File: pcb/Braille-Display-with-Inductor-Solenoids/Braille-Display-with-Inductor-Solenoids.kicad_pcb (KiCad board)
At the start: 2 copper layers, 100 x 100 mm, 190 parts, among them J1 Screw_Terminal_01x02, J2 Screw_Terminal_01x02, J3 Screw_Terminal_01x02, SW1 SW_Push, SW2 SW_Push, U1 RP2040-Zero, U10 AD116, U11 AD116, U12 AD116, U13 AD116, U14 AD116, U15 AD116, U16 AD116, U17 AD116, U18 AD116, U19 AD116, U2 AD116, U20 AD116, U21 AD116, U22 AD116, U23 AD116, U24 AD116, U25 AD116, U3 AD116, U4 AD116, U5 AD116, U6 AD116, U7 AD116, U8 AD116, U9 AD116

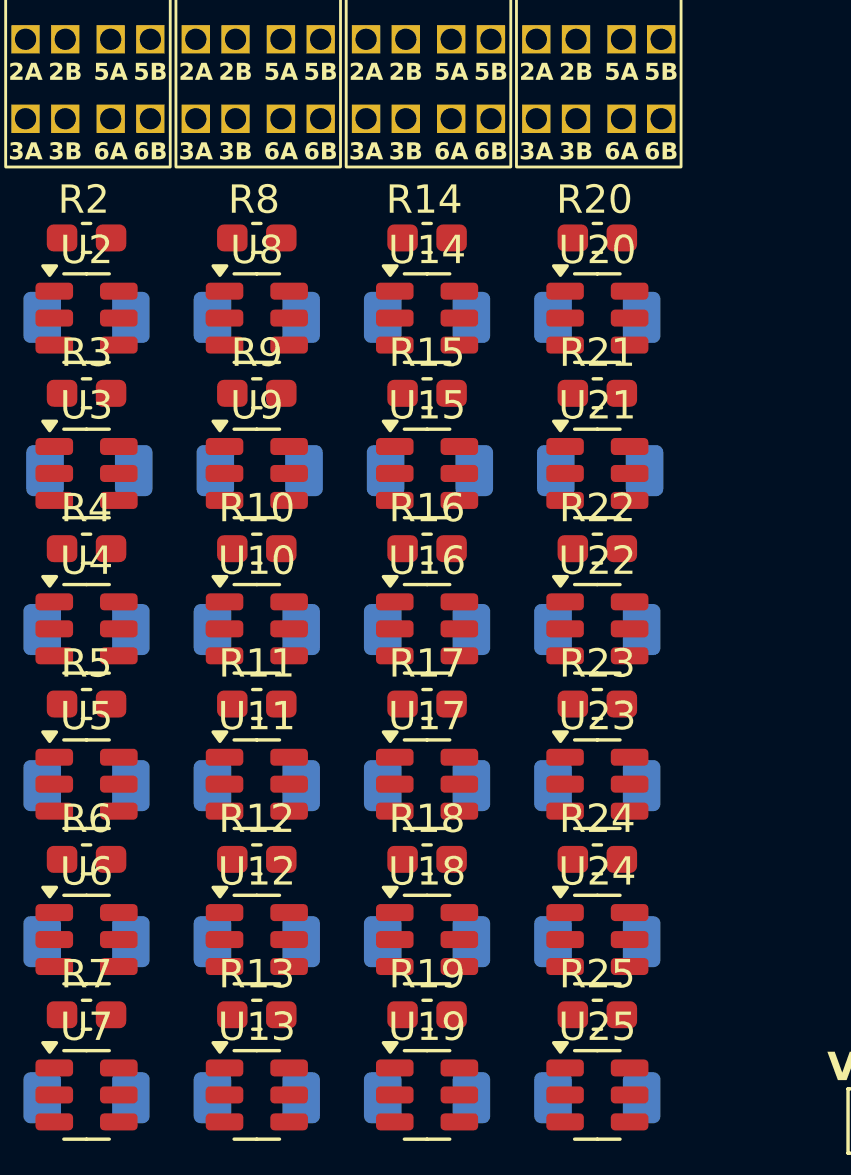
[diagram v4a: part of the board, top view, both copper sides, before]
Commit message: Change page layout and reconnect components
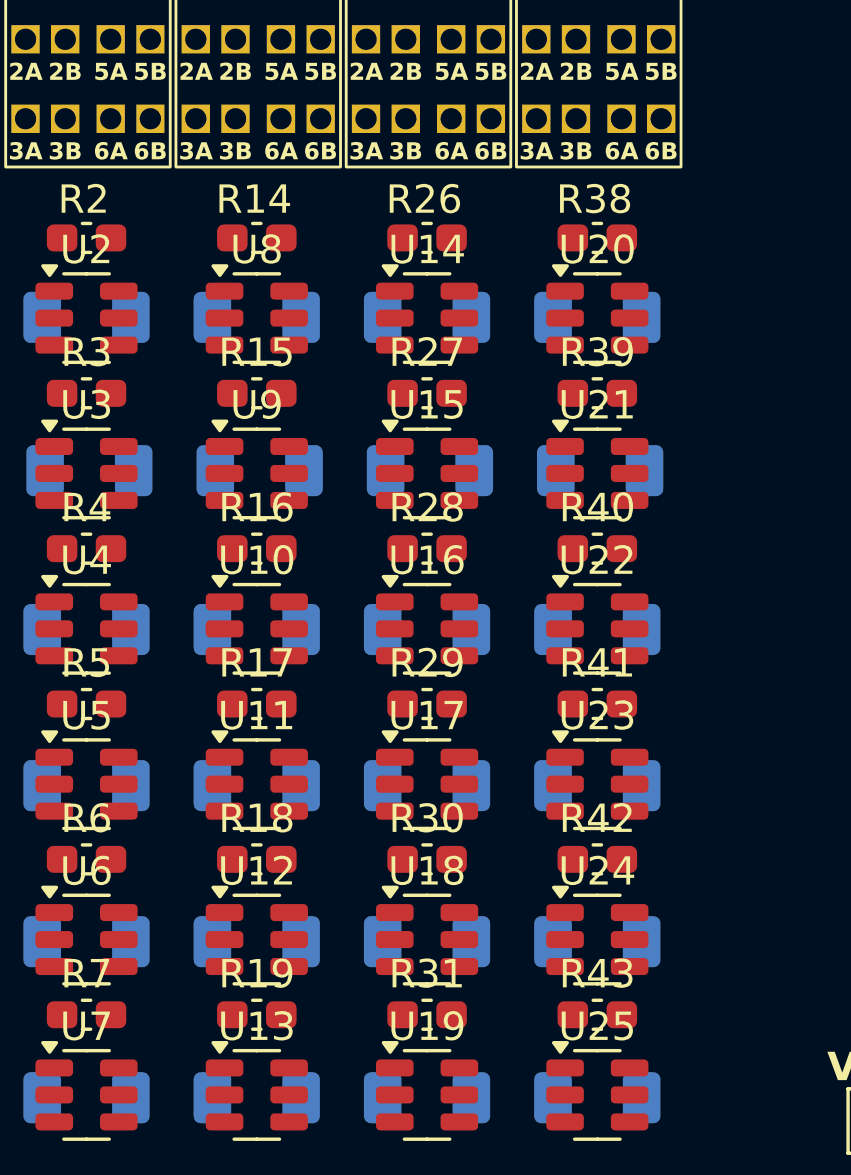
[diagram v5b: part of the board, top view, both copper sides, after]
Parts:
- R10, R11, R12, R13, R20, R21, R22, R23, R24, R25, R8, R9: value 20 -> 5k1; footprint Capacitor_SMD:C_0603_1608Metric_Pad1.08x0.95mm_HandSolder -> Resistor_SMD:R_0603_1608Metric; moved to B.Cu
- R26, R27, R28, R29, R30, R31, R38, R39, R40, R41, R42, R43: value 5k1 -> 20; footprint Resistor_SMD:R_0603_1608Metric -> Capacitor_SMD:C_0603_1608Metric_Pad1.08x0.95mm_HandSolder; moved to F.Cu
- moved R38 40.5 mm to (69.2, 71.0), turned to 180 degrees
- moved R20 36.5 mm to (57.2, 105.5)
- moved R26 36.5 mm to (63.2, 71.0)
- moved R8 35.0 mm to (51.2, 105.5)
- moved R21 34.9 mm to (57.1, 109.2), turned to 180 degrees
- moved R9 33.3 mm to (51.1, 109.2), turned to 180 degrees
- moved R22 33.2 mm to (57.1, 112.9), turned to 180 degrees
- moved R39 33.1 mm to (69.2, 76.5)
- moved C5 32.9 mm to (51.2, 101.3)
- moved R10 31.5 mm to (51.1, 112.9), turned to 180 degrees
- moved R27 29.6 mm to (63.2, 76.5), turned to 0 degrees
- moved R40 26.1 mm to (69.2, 82.0)
- moved R42 25.6 mm to (69.2, 92.9)
- moved C4 25.1 mm to (51.2, 95.8)
- moved R28 23.5 mm to (63.2, 82.0), turned to 0 degrees
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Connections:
- net /Braille_Cell/DOT1_A renamed /Braille_Cells_and_Controls/Braille_Cell/DOT1_A
- net /Braille_Cell/DOT1_B renamed /Braille_Cells_and_Controls/Braille_Cell/DOT1_B
- net /Braille_Cell/DOT1_B_CTRL renamed /Braille_Cells_and_Controls/CELL0_DOT1_B
- net /Braille_Cell/DOT2_A renamed /Braille_Cells_and_Controls/Braille_Cell/DOT2_A
- net /Braille_Cell/DOT2_B renamed /Braille_Cells_and_Controls/Braille_Cell/DOT2_B
- net /Braille_Cell/DOT3_A renamed /Braille_Cells_and_Controls/Braille_Cell/DOT3_A
- net /Braille_Cell/DOT3_B renamed /Braille_Cells_and_Controls/Braille_Cell/DOT3_B
- net /Braille_Cell/DOT4_A renamed /Braille_Cells_and_Controls/Braille_Cell/DOT4_A
- net /Braille_Cell/DOT4_B renamed /Braille_Cells_and_Controls/Braille_Cell/DOT4_B
- net /Braille_Cell/DOT5_A renamed /Braille_Cells_and_Controls/Braille_Cell/DOT5_A
- net /Braille_Cell/DOT5_B renamed /Braille_Cells_and_Controls/Braille_Cell/DOT5_B
- net /Braille_Cell/DOT6_A renamed /Braille_Cells_and_Controls/Braille_Cell/DOT6_A
- net /Braille_Cell/DOT6_B renamed /Braille_Cells_and_Controls/Braille_Cell/DOT6_B
- net /Braille_Cell1/DOT1_A renamed /Braille_Cells_and_Controls/Braille_Cell1/DOT1_A
- net /Braille_Cell1/DOT2_A renamed /Braille_Cells_and_Controls/Braille_Cell1/DOT2_A
- net /Braille_Cell1/DOT3_A renamed /Braille_Cells_and_Controls/Braille_Cell1/DOT3_A
- net /Braille_Cell1/DOT4_A renamed /Braille_Cells_and_Controls/Braille_Cell1/DOT4_A
- net /Braille_Cell1/DOT5_A renamed /Braille_Cells_and_Controls/Braille_Cell1/DOT5_A
- net /Braille_Cell1/DOT6_A renamed /Braille_Cells_and_Controls/Braille_Cell1/DOT6_A
- net /Braille_Cell2/DOT1_A renamed /Braille_Cells_and_Controls/Braille_Cell2/DOT1_A
- net /Braille_Cell2/DOT2_A renamed /Braille_Cells_and_Controls/Braille_Cell2/DOT2_A
- net /Braille_Cell2/DOT3_A renamed /Braille_Cells_and_Controls/Braille_Cell2/DOT3_A
- net /Braille_Cell2/DOT4_A renamed /Braille_Cells_and_Controls/Braille_Cell2/DOT4_A
- net /Braille_Cell2/DOT5_A renamed /Braille_Cells_and_Controls/Braille_Cell2/DOT5_A
- net /Braille_Cell2/DOT6_A renamed /Braille_Cells_and_Controls/Braille_Cell2/DOT6_A
- net /Braille_Cell3/DOT1_A renamed /Braille_Cells_and_Controls/Braille_Cell3/DOT1_A
- net /Braille_Cell3/DOT2_A renamed /Braille_Cells_and_Controls/Braille_Cell3/DOT2_A
- net /Braille_Cell3/DOT3_A renamed /Braille_Cells_and_Controls/Braille_Cell3/DOT3_A
- net /Braille_Cell3/DOT4_A renamed /Braille_Cells_and_Controls/Braille_Cell3/DOT4_A
- net /Braille_Cell3/DOT5_A renamed /Braille_Cells_and_Controls/Braille_Cell3/DOT5_A
- net /Braille_Cell3/DOT6_A renamed /Braille_Cells_and_Controls/Braille_Cell3/DOT6_A
- net /Braille_Cell3/DOT6_A_CTRL renamed /Braille_Cells_and_Controls/CELL3_DOT6_A
- net /Braille_Cell3/DOT6_B_CTRL renamed /Braille_Cells_and_Controls/CELL3_DOT6_B
- D10 pad 1: /Braille_Cell/DOT2_B_CTRL -> /Braille_Cells_and_Controls/CELL1_DOT3_B
- D11 pad 1: /Braille_Cell/DOT5_B_CTRL -> /Braille_Cells_and_Controls/CELL1_DOT4_B
- D12 pad 1: /Braille_Cell1/DOT2_B_CTRL -> /Braille_Cells_and_Controls/CELL1_DOT5_B
- D13 pad 1: /Braille_Cell1/DOT5_B_CTRL -> /Braille_Cells_and_Controls/CELL1_DOT6_B
- D14 pad 1: /Braille_Cell2/DOT2_B_CTRL -> /Braille_Cells_and_Controls/CELL2_DOT1_B
- D15 pad 1: /Braille_Cell2/DOT5_B_CTRL -> /Braille_Cells_and_Controls/CELL2_DOT2_B
- D16 pad 1: /Braille_Cell3/DOT2_B_CTRL -> /Braille_Cells_and_Controls/CELL2_DOT3_B
- D17 pad 1: /Braille_Cell3/DOT5_B_CTRL -> /Braille_Cells_and_Controls/CELL2_DOT4_B
- D18 pad 1: /Braille_Cell/DOT3_B_CTRL -> /Braille_Cells_and_Controls/CELL2_DOT5_B
- D19 pad 1: /Braille_Cell/DOT6_B_CTRL -> /Braille_Cells_and_Controls/CELL2_DOT6_B
- D20 pad 1: /Braille_Cell1/DOT3_B_CTRL -> /Braille_Cells_and_Controls/CELL3_DOT1_B
- D21 pad 1: /Braille_Cell1/DOT6_B_CTRL -> /Braille_Cells_and_Controls/CELL3_DOT2_B
- D22 pad 1: /Braille_Cell2/DOT3_B_CTRL -> /Braille_Cells_and_Controls/CELL3_DOT3_B
- D23 pad 1: /Braille_Cell2/DOT6_B_CTRL -> /Braille_Cells_and_Controls/CELL3_DOT4_B
- D24 pad 1: /Braille_Cell3/DOT3_B_CTRL -> /Braille_Cells_and_Controls/CELL3_DOT5_B
- D3 pad 1: /Braille_Cell1/DOT1_B_CTRL -> /Braille_Cells_and_Controls/CELL0_DOT2_B
- D4 pad 1: /Braille_Cell2/DOT1_B_CTRL -> /Braille_Cells_and_Controls/CELL0_DOT3_B
- D5 pad 1: /Braille_Cell3/DOT1_B_CTRL -> /Braille_Cells_and_Controls/CELL0_DOT4_B
- D6 pad 1: /Braille_Cell/DOT4_B_CTRL -> /Braille_Cells_and_Controls/CELL0_DOT5_B
- D7 pad 1: /Braille_Cell1/DOT4_B_CTRL -> /Braille_Cells_and_Controls/CELL0_DOT6_B
- D8 pad 1: /Braille_Cell2/DOT4_B_CTRL -> /Braille_Cells_and_Controls/CELL1_DOT1_B
- D9 pad 1: /Braille_Cell3/DOT4_B_CTRL -> /Braille_Cells_and_Controls/CELL1_DOT2_B
- R10 pad 1: /Braille_Cell1/DOT3_B -> /Braille_Cells_and_Controls/CELL0_DOT3_A
- R10 pad 2: Net-(B2-3B) -> Net-(D4-AK)
- R11 pad 1: Net-(B2-4B) -> /Braille_Cells_and_Controls/CELL0_DOT4_A
- R11 pad 2: /Braille_Cell1/DOT4_B -> Net-(D5-AK)
- R12 pad 1: Net-(B2-5B) -> /Braille_Cells_and_Controls/CELL0_DOT5_A
- R12 pad 2: /Braille_Cell1/DOT5_B -> Net-(D6-AK)
- R13 pad 1: Net-(B2-6B) -> /Braille_Cells_and_Controls/CELL0_DOT6_A
- R13 pad 2: /Braille_Cell1/DOT6_B -> Net-(D7-AK)
- R14 pad 1: /Braille_Cell2/DOT1_B -> /Braille_Cells_and_Controls/Braille_Cell1/DOT1_B
- R14 pad 2: Net-(B3-1B) -> Net-(B2-1B)
- R15 pad 1: /Braille_Cell2/DOT2_B -> /Braille_Cells_and_Controls/Braille_Cell1/DOT2_B
- R15 pad 2: Net-(B3-2B) -> Net-(B2-2B)
- R16 pad 1: /Braille_Cell2/DOT3_B -> /Braille_Cells_and_Controls/Braille_Cell1/DOT3_B
- R16 pad 2: Net-(B3-3B) -> Net-(B2-3B)
- R17 pad 1: Net-(B3-4B) -> Net-(B2-4B)
- R17 pad 2: /Braille_Cell2/DOT4_B -> /Braille_Cells_and_Controls/Braille_Cell1/DOT4_B
- R18 pad 1: Net-(B3-5B) -> Net-(B2-5B)
- R18 pad 2: /Braille_Cell2/DOT5_B -> /Braille_Cells_and_Controls/Braille_Cell1/DOT5_B
- R19 pad 1: Net-(B3-6B) -> Net-(B2-6B)
- R19 pad 2: /Braille_Cell2/DOT6_B -> /Braille_Cells_and_Controls/Braille_Cell1/DOT6_B
- R20 pad 1: /Braille_Cell3/DOT1_B -> /Braille_Cells_and_Controls/CELL1_DOT1_A
- R20 pad 2: Net-(B4-1B) -> Net-(D8-AK)
- R21 pad 1: /Braille_Cell3/DOT2_B -> /Braille_Cells_and_Controls/CELL1_DOT2_A
- R21 pad 2: Net-(B4-2B) -> Net-(D9-AK)
- R22 pad 1: /Braille_Cell3/DOT3_B -> /Braille_Cells_and_Controls/CELL1_DOT3_A
- R22 pad 2: Net-(B4-3B) -> Net-(D10-AK)
- R23 pad 1: Net-(B4-4B) -> /Braille_Cells_and_Controls/CELL1_DOT4_A
- R23 pad 2: /Braille_Cell3/DOT4_B -> Net-(D11-AK)
- R24 pad 1: Net-(B4-5B) -> /Braille_Cells_and_Controls/CELL1_DOT5_A
- R24 pad 2: /Braille_Cell3/DOT5_B -> Net-(D12-AK)
- R25 pad 1: Net-(B4-6B) -> /Braille_Cells_and_Controls/CELL1_DOT6_A
- R25 pad 2: /Braille_Cell3/DOT6_B -> Net-(D13-AK)
- R26 pad 1: /Braille_Cell/DOT1_A_CTRL -> /Braille_Cells_and_Controls/Braille_Cell2/DOT1_B
- R26 pad 2: Net-(D2-AK) -> Net-(B3-1B)
- R27 pad 1: /Braille_Cell1/DOT1_A_CTRL -> /Braille_Cells_and_Controls/Braille_Cell2/DOT2_B
- R27 pad 2: Net-(D3-AK) -> Net-(B3-2B)
- R28 pad 1: /Braille_Cell2/DOT1_A_CTRL -> /Braille_Cells_and_Controls/Braille_Cell2/DOT3_B
- R28 pad 2: Net-(D4-AK) -> Net-(B3-3B)
- R29 pad 1: /Braille_Cell3/DOT1_A_CTRL -> Net-(B3-4B)
- R29 pad 2: Net-(D5-AK) -> /Braille_Cells_and_Controls/Braille_Cell2/DOT4_B
- R30 pad 1: /Braille_Cell/DOT2_A_CTRL -> Net-(B3-5B)
- R30 pad 2: Net-(D10-AK) -> /Braille_Cells_and_Controls/Braille_Cell2/DOT5_B
- R31 pad 1: /Braille_Cell1/DOT2_A_CTRL -> Net-(B3-6B)
- R31 pad 2: Net-(D12-AK) -> /Braille_Cells_and_Controls/Braille_Cell2/DOT6_B
- R32 pad 1: /Braille_Cell2/DOT2_A_CTRL -> /Braille_Cells_and_Controls/CELL2_DOT1_A
- R33 pad 1: /Braille_Cell3/DOT2_A_CTRL -> /Braille_Cells_and_Controls/CELL2_DOT2_A
- R33 pad 2: Net-(D16-AK) -> Net-(D15-AK)
- R34 pad 1: /Braille_Cell/DOT3_A_CTRL -> /Braille_Cells_and_Controls/CELL2_DOT3_A
- R34 pad 2: Net-(D18-AK) -> Net-(D16-AK)
- R35 pad 1: /Braille_Cell1/DOT3_A_CTRL -> /Braille_Cells_and_Controls/CELL2_DOT4_A
- R35 pad 2: Net-(D20-AK) -> Net-(D17-AK)
- R36 pad 1: /Braille_Cell2/DOT3_A_CTRL -> /Braille_Cells_and_Controls/CELL2_DOT5_A
- R36 pad 2: Net-(D22-AK) -> Net-(D18-AK)
- R37 pad 1: /Braille_Cell3/DOT3_A_CTRL -> /Braille_Cells_and_Controls/CELL2_DOT6_A
- R37 pad 2: Net-(D24-AK) -> Net-(D19-AK)
- R38 pad 1: /Braille_Cell/DOT4_A_CTRL -> /Braille_Cells_and_Controls/Braille_Cell3/DOT1_B
- R38 pad 2: Net-(D6-AK) -> Net-(B4-1B)
- R39 pad 1: /Braille_Cell1/DOT4_A_CTRL -> /Braille_Cells_and_Controls/Braille_Cell3/DOT2_B
- R39 pad 2: Net-(D7-AK) -> Net-(B4-2B)
- R40 pad 1: /Braille_Cell2/DOT4_A_CTRL -> /Braille_Cells_and_Controls/Braille_Cell3/DOT3_B
- R40 pad 2: Net-(D8-AK) -> Net-(B4-3B)
- R41 pad 1: /Braille_Cell3/DOT4_A_CTRL -> Net-(B4-4B)
- R41 pad 2: Net-(D9-AK) -> /Braille_Cells_and_Controls/Braille_Cell3/DOT4_B
- R42 pad 1: /Braille_Cell/DOT5_A_CTRL -> Net-(B4-5B)
- R42 pad 2: Net-(D11-AK) -> /Braille_Cells_and_Controls/Braille_Cell3/DOT5_B
- R43 pad 1: /Braille_Cell1/DOT5_A_CTRL -> Net-(B4-6B)
- R43 pad 2: Net-(D13-AK) -> /Braille_Cells_and_Controls/Braille_Cell3/DOT6_B
- R44 pad 1: /Braille_Cell2/DOT5_A_CTRL -> /Braille_Cells_and_Controls/CELL3_DOT1_A
- R44 pad 2: Net-(D15-AK) -> Net-(D20-AK)
- R45 pad 1: /Braille_Cell3/DOT5_A_CTRL -> /Braille_Cells_and_Controls/CELL3_DOT2_A
- R45 pad 2: Net-(D17-AK) -> Net-(D21-AK)
- R46 pad 1: /Braille_Cell/DOT6_A_CTRL -> /Braille_Cells_and_Controls/CELL3_DOT3_A
- R46 pad 2: Net-(D19-AK) -> Net-(D22-AK)
- R47 pad 1: /Braille_Cell1/DOT6_A_CTRL -> /Braille_Cells_and_Controls/CELL3_DOT4_A
- R47 pad 2: Net-(D21-AK) -> Net-(D23-AK)
- R48 pad 1: /Braille_Cell2/DOT6_A_CTRL -> /Braille_Cells_and_Controls/CELL3_DOT5_A
- R48 pad 2: Net-(D23-AK) -> Net-(D24-AK)
- R8 pad 1: /Braille_Cell1/DOT1_B -> /Braille_Cells_and_Controls/CELL0_DOT1_A
- R8 pad 2: Net-(B2-1B) -> Net-(D2-AK)
- R9 pad 1: /Braille_Cell1/DOT2_B -> /Braille_Cells_and_Controls/CELL0_DOT2_A
- R9 pad 2: Net-(B2-2B) -> Net-(D3-AK)
- U1 pad 14: /SHIFT_RCLK -> /~{SHIFT_SRCLR}
- U1 pad 15: /SHIFT_G -> /SHIFT_RCLK
- U1 pad 16: unconnected-(U1-GP6-Pad16)_1 -> /~{SHIFT_OE}
- U10 pad 1: /Braille_Cell1/DOT3_B -> /Braille_Cells_and_Controls/Braille_Cell1/DOT3_B
- U10 pad 3: /Braille_Cell1/DOT3_B_CTRL -> /Braille_Cells_and_Controls/CELL1_DOT3_B
- U10 pad 4: /Braille_Cell1/DOT3_A_CTRL -> /Braille_Cells_and_Controls/CELL1_DOT3_A
- U11 pad 1: /Braille_Cell1/DOT4_B -> /Braille_Cells_and_Controls/Braille_Cell1/DOT4_B
- U11 pad 3: /Braille_Cell1/DOT4_B_CTRL -> /Braille_Cells_and_Controls/CELL1_DOT4_B
- U11 pad 4: /Braille_Cell1/DOT4_A_CTRL -> /Braille_Cells_and_Controls/CELL1_DOT4_A
- U12 pad 1: /Braille_Cell1/DOT5_B -> /Braille_Cells_and_Controls/Braille_Cell1/DOT5_B
- U12 pad 3: /Braille_Cell1/DOT5_B_CTRL -> /Braille_Cells_and_Controls/CELL1_DOT5_B
- U12 pad 4: /Braille_Cell1/DOT5_A_CTRL -> /Braille_Cells_and_Controls/CELL1_DOT5_A
- U13 pad 1: /Braille_Cell1/DOT6_B -> /Braille_Cells_and_Controls/Braille_Cell1/DOT6_B
- U13 pad 3: /Braille_Cell1/DOT6_B_CTRL -> /Braille_Cells_and_Controls/CELL1_DOT6_B
- U13 pad 4: /Braille_Cell1/DOT6_A_CTRL -> /Braille_Cells_and_Controls/CELL1_DOT6_A
- U14 pad 1: /Braille_Cell2/DOT1_B -> /Braille_Cells_and_Controls/Braille_Cell2/DOT1_B
- U14 pad 3: /Braille_Cell2/DOT1_B_CTRL -> /Braille_Cells_and_Controls/CELL2_DOT1_B
- U14 pad 4: /Braille_Cell2/DOT1_A_CTRL -> /Braille_Cells_and_Controls/CELL2_DOT1_A
- U15 pad 1: /Braille_Cell2/DOT2_B -> /Braille_Cells_and_Controls/Braille_Cell2/DOT2_B
- U15 pad 3: /Braille_Cell2/DOT2_B_CTRL -> /Braille_Cells_and_Controls/CELL2_DOT2_B
- U15 pad 4: /Braille_Cell2/DOT2_A_CTRL -> /Braille_Cells_and_Controls/CELL2_DOT2_A
- U16 pad 1: /Braille_Cell2/DOT3_B -> /Braille_Cells_and_Controls/Braille_Cell2/DOT3_B
- U16 pad 3: /Braille_Cell2/DOT3_B_CTRL -> /Braille_Cells_and_Controls/CELL2_DOT3_B
- U16 pad 4: /Braille_Cell2/DOT3_A_CTRL -> /Braille_Cells_and_Controls/CELL2_DOT3_A
- U17 pad 1: /Braille_Cell2/DOT4_B -> /Braille_Cells_and_Controls/Braille_Cell2/DOT4_B
- U17 pad 3: /Braille_Cell2/DOT4_B_CTRL -> /Braille_Cells_and_Controls/CELL2_DOT4_B
- U17 pad 4: /Braille_Cell2/DOT4_A_CTRL -> /Braille_Cells_and_Controls/CELL2_DOT4_A
- U18 pad 1: /Braille_Cell2/DOT5_B -> /Braille_Cells_and_Controls/Braille_Cell2/DOT5_B
- U18 pad 3: /Braille_Cell2/DOT5_B_CTRL -> /Braille_Cells_and_Controls/CELL2_DOT5_B
- U18 pad 4: /Braille_Cell2/DOT5_A_CTRL -> /Braille_Cells_and_Controls/CELL2_DOT5_A
- U19 pad 1: /Braille_Cell2/DOT6_B -> /Braille_Cells_and_Controls/Braille_Cell2/DOT6_B
- U19 pad 3: /Braille_Cell2/DOT6_B_CTRL -> /Braille_Cells_and_Controls/CELL2_DOT6_B
- U19 pad 4: /Braille_Cell2/DOT6_A_CTRL -> /Braille_Cells_and_Controls/CELL2_DOT6_A
- U2 pad 4: /Braille_Cell/DOT1_A_CTRL -> /Braille_Cells_and_Controls/CELL0_DOT1_A
- U20 pad 1: /Braille_Cell3/DOT1_B -> /Braille_Cells_and_Controls/Braille_Cell3/DOT1_B
- U20 pad 3: /Braille_Cell3/DOT1_B_CTRL -> /Braille_Cells_and_Controls/CELL3_DOT1_B
- U20 pad 4: /Braille_Cell3/DOT1_A_CTRL -> /Braille_Cells_and_Controls/CELL3_DOT1_A
- U21 pad 1: /Braille_Cell3/DOT2_B -> /Braille_Cells_and_Controls/Braille_Cell3/DOT2_B
- U21 pad 3: /Braille_Cell3/DOT2_B_CTRL -> /Braille_Cells_and_Controls/CELL3_DOT2_B
- U21 pad 4: /Braille_Cell3/DOT2_A_CTRL -> /Braille_Cells_and_Controls/CELL3_DOT2_A
- U22 pad 1: /Braille_Cell3/DOT3_B -> /Braille_Cells_and_Controls/Braille_Cell3/DOT3_B
- U22 pad 3: /Braille_Cell3/DOT3_B_CTRL -> /Braille_Cells_and_Controls/CELL3_DOT3_B
- U22 pad 4: /Braille_Cell3/DOT3_A_CTRL -> /Braille_Cells_and_Controls/CELL3_DOT3_A
- U23 pad 1: /Braille_Cell3/DOT4_B -> /Braille_Cells_and_Controls/Braille_Cell3/DOT4_B
- U23 pad 3: /Braille_Cell3/DOT4_B_CTRL -> /Braille_Cells_and_Controls/CELL3_DOT4_B
- U23 pad 4: /Braille_Cell3/DOT4_A_CTRL -> /Braille_Cells_and_Controls/CELL3_DOT4_A
- U24 pad 1: /Braille_Cell3/DOT5_B -> /Braille_Cells_and_Controls/Braille_Cell3/DOT5_B
- U24 pad 3: /Braille_Cell3/DOT5_B_CTRL -> /Braille_Cells_and_Controls/CELL3_DOT5_B
- U24 pad 4: /Braille_Cell3/DOT5_A_CTRL -> /Braille_Cells_and_Controls/CELL3_DOT5_A
- U25 pad 1: /Braille_Cell3/DOT6_B -> /Braille_Cells_and_Controls/Braille_Cell3/DOT6_B
- U3 pad 3: /Braille_Cell/DOT2_B_CTRL -> /Braille_Cells_and_Controls/CELL0_DOT2_B
- U3 pad 4: /Braille_Cell/DOT2_A_CTRL -> /Braille_Cells_and_Controls/CELL0_DOT2_A
- U4 pad 3: /Braille_Cell/DOT3_B_CTRL -> /Braille_Cells_and_Controls/CELL0_DOT3_B
- U4 pad 4: /Braille_Cell/DOT3_A_CTRL -> /Braille_Cells_and_Controls/CELL0_DOT3_A
- U5 pad 3: /Braille_Cell/DOT4_B_CTRL -> /Braille_Cells_and_Controls/CELL0_DOT4_B
- U5 pad 4: /Braille_Cell/DOT4_A_CTRL -> /Braille_Cells_and_Controls/CELL0_DOT4_A
- U6 pad 3: /Braille_Cell/DOT5_B_CTRL -> /Braille_Cells_and_Controls/CELL0_DOT5_B
- U6 pad 4: /Braille_Cell/DOT5_A_CTRL -> /Braille_Cells_and_Controls/CELL0_DOT5_A
- U7 pad 3: /Braille_Cell/DOT6_B_CTRL -> /Braille_Cells_and_Controls/CELL0_DOT6_B
- U7 pad 4: /Braille_Cell/DOT6_A_CTRL -> /Braille_Cells_and_Controls/CELL0_DOT6_A
- U8 pad 1: /Braille_Cell1/DOT1_B -> /Braille_Cells_and_Controls/Braille_Cell1/DOT1_B
- U8 pad 3: /Braille_Cell1/DOT1_B_CTRL -> /Braille_Cells_and_Controls/CELL1_DOT1_B
- U8 pad 4: /Braille_Cell1/DOT1_A_CTRL -> /Braille_Cells_and_Controls/CELL1_DOT1_A
- U9 pad 1: /Braille_Cell1/DOT2_B -> /Braille_Cells_and_Controls/Braille_Cell1/DOT2_B
- U9 pad 3: /Braille_Cell1/DOT2_B_CTRL -> /Braille_Cells_and_Controls/CELL1_DOT2_B
- U9 pad 4: /Braille_Cell1/DOT2_A_CTRL -> /Braille_Cells_and_Controls/CELL1_DOT2_A

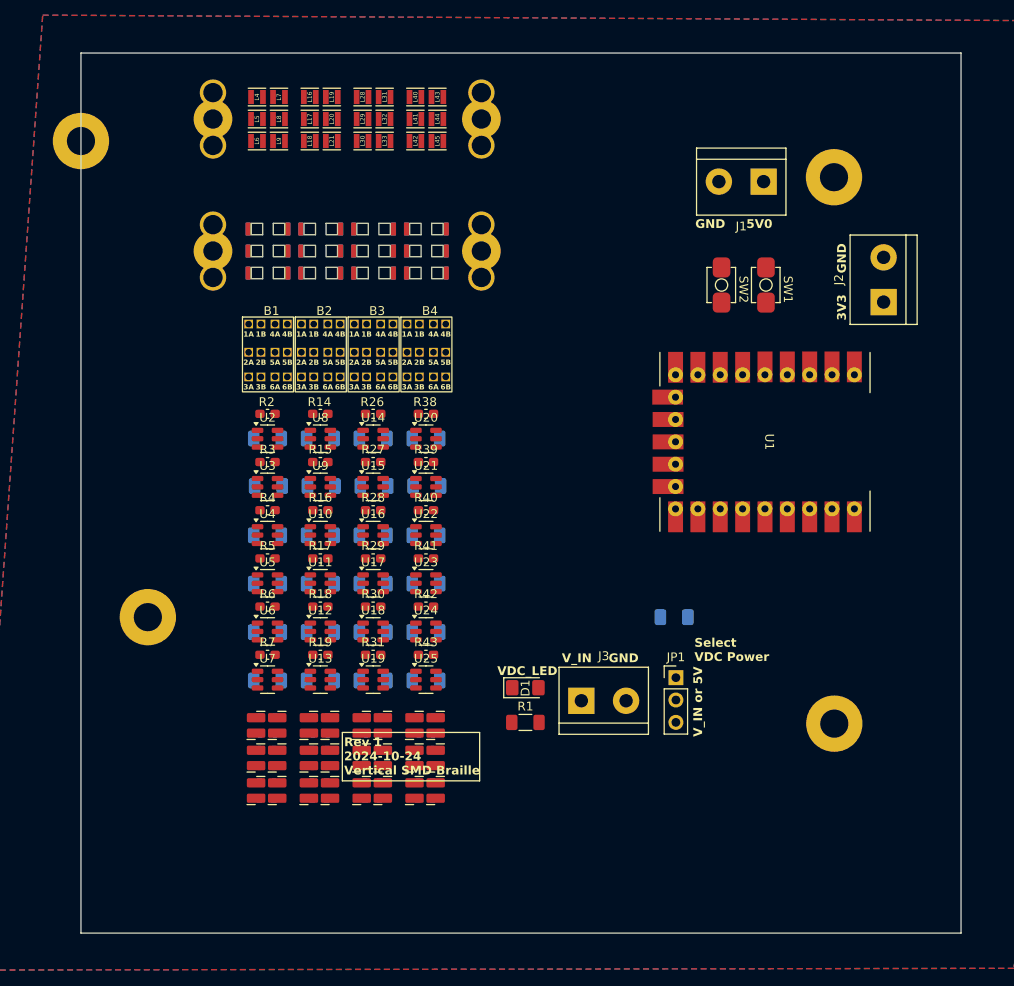
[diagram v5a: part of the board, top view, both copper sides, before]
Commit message: Layout debugging components
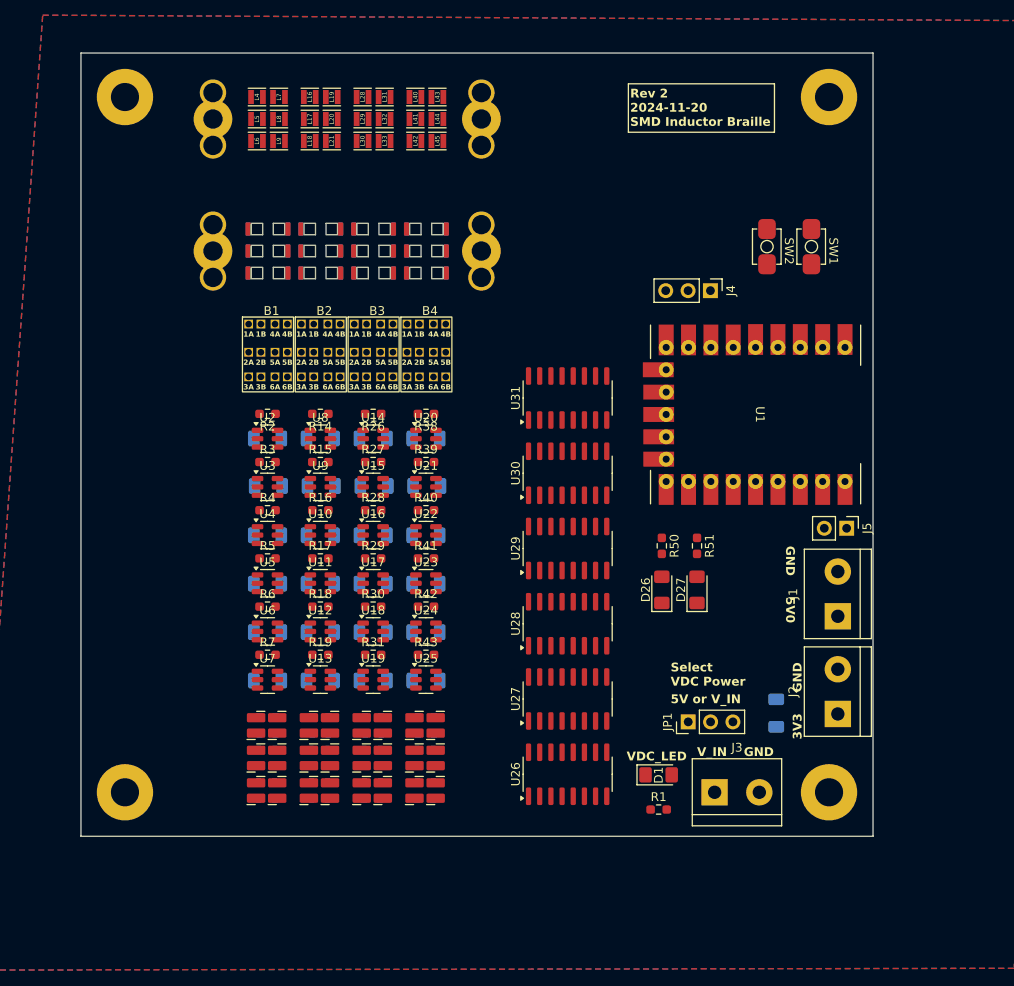
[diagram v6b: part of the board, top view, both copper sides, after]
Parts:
- added D26: LED, LED_SMD:LED_1206_3216Metric_Pad1.42x1.75mm_HandSolder, F.Cu at (96.0, 91.0)
- added D27: LED, LED_SMD:LED_1206_3216Metric_Pad1.42x1.75mm_HandSolder, F.Cu at (100.0, 91.0)
- added J4: Conn_01x03, Connector_PinHeader_2.54mm:PinHeader_1x03_P2.54mm_Vertical, F.Cu at (101.5, 57.0)
- added J5: Conn_01x02, Connector_PinHeader_2.54mm:PinHeader_1x02_P2.54mm_Vertical, F.Cu at (117.0, 84.0)
- added R50: 5k1, Resistor_SMD:R_0603_1608Metric_Pad0.98x0.95mm_HandSolder, F.Cu at (96.0, 86.0)
- added R51: 5k1, Resistor_SMD:R_0603_1608Metric_Pad0.98x0.95mm_HandSolder, F.Cu at (100.0, 86.0)
- added U26: 74HC595, Package_SO:SOP-16_3.9x9.9mm_P1.27mm, F.Cu at (85.3, 112.0)
- added U27: 74HC595, Package_SO:SOP-16_3.9x9.9mm_P1.27mm, F.Cu at (85.3, 103.4)
- added U28: 74HC595, Package_SO:SOP-16_3.9x9.9mm_P1.27mm, F.Cu at (85.3, 94.8)
- added U29: 74HC595, Package_SO:SOP-16_3.9x9.9mm_P1.27mm, F.Cu at (85.3, 86.3)
- added U30: 74HC595, Package_SO:SOP-16_3.9x9.9mm_P1.27mm, F.Cu at (85.3, 77.8)
- added U31: 74HC595, Package_SO:SOP-16_3.9x9.9mm_P1.27mm, F.Cu at (85.3, 69.2)
- R1: footprint Resistor_SMD:R_1206_3216Metric_Pad1.30x1.75mm_HandSolder -> Resistor_SMD:R_0603_1608Metric_Pad0.98x0.95mm_HandSolder
- R10, R11, R12, R13, R20, R21, R22, R23, R24, R25, R32, R33, R34, R35, R36, R37, R44, R45, R46, R47, R48, R49, R8, R9: footprint Resistor_SMD:R_0603_1608Metric -> Resistor_SMD:R_0603_1608Metric_Pad0.98x0.95mm_HandSolder
- R14, R15, R16, R17, R18, R19, R2, R26, R27, R28, R29, R3, R30, R31, R38, R39, R4, R40, R41, R42, R43, R5, R6, R7: footprint Capacitor_SMD:C_0603_1608Metric_Pad1.08x0.95mm_HandSolder -> Resistor_SMD:R_0603_1608Metric_Pad0.98x0.95mm_HandSolder
- moved J1 50.1 mm to (116.0, 94.0), turned to 90 degrees
- moved J2 47.1 mm to (116.0, 105.1)
- moved H3 20.1 mm to (35.0, 114.0)
- moved J3 18.4 mm to (102.0, 114.0)
- moved D1 18.1 mm to (95.6, 112.0)
- moved R1 18.1 mm to (95.6, 116.0)
- moved C1 15.9 mm to (109.0, 105.0), turned to -90 degrees
- moved H2 9.13 mm to (115.0, 35.0)
- moved H4 7.82 mm to (115.0, 114.0)
- moved H1 7.07 mm to (35.0, 35.0)
- moved SW2 6.76 mm to (108.0, 52.0)
- moved SW1 6.76 mm to (113.0, 52.0)
- moved JP1 5.22 mm to (99.0, 106.0), turned to 90 degrees
- moved U1 3.29 mm to (93.8, 60.9)
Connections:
- U1 pad 10: unconnected-(U1-GP0-Pad10) -> Net-(J5-Pin_1)
- U1 pad 11: unconnected-(U1-GP1-Pad11)_1 -> Net-(J5-Pin_2)
- U1 pad 17: unconnected-(U1-GP7-Pad17)_1 -> /GP_LED_0
- U1 pad 18: unconnected-(U1-GP8-Pad18) -> /GP_LED_1
- U1 pad 7: unconnected-(U1-GP26-Pad7)_1 -> Net-(J4-Pin_1)
- U1 pad 8: unconnected-(U1-GP15-Pad8) -> Net-(J4-Pin_2)
- U1 pad 9: unconnected-(U1-GP14-Pad9) -> Net-(J4-Pin_3)
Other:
- board size 100 x 100 mm -> 90 x 89 mm
- board text added: "5V or V_IN"
- board text added: "Rev 2 2024-11-20 SMD Inductor Braille"
- board text removed: "Rev 1 2024-10-24 Vertical SMD Braille"
- board text removed: "V_IN or 5V"

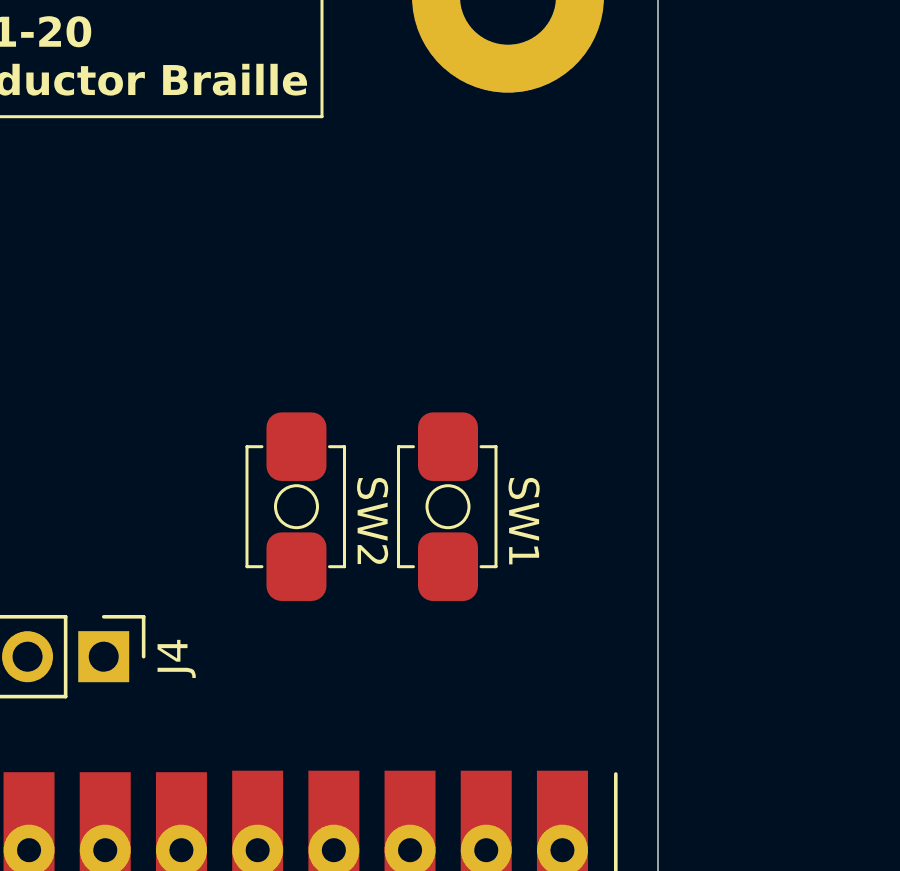
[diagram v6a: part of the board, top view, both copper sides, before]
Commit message: Add UART soicbite
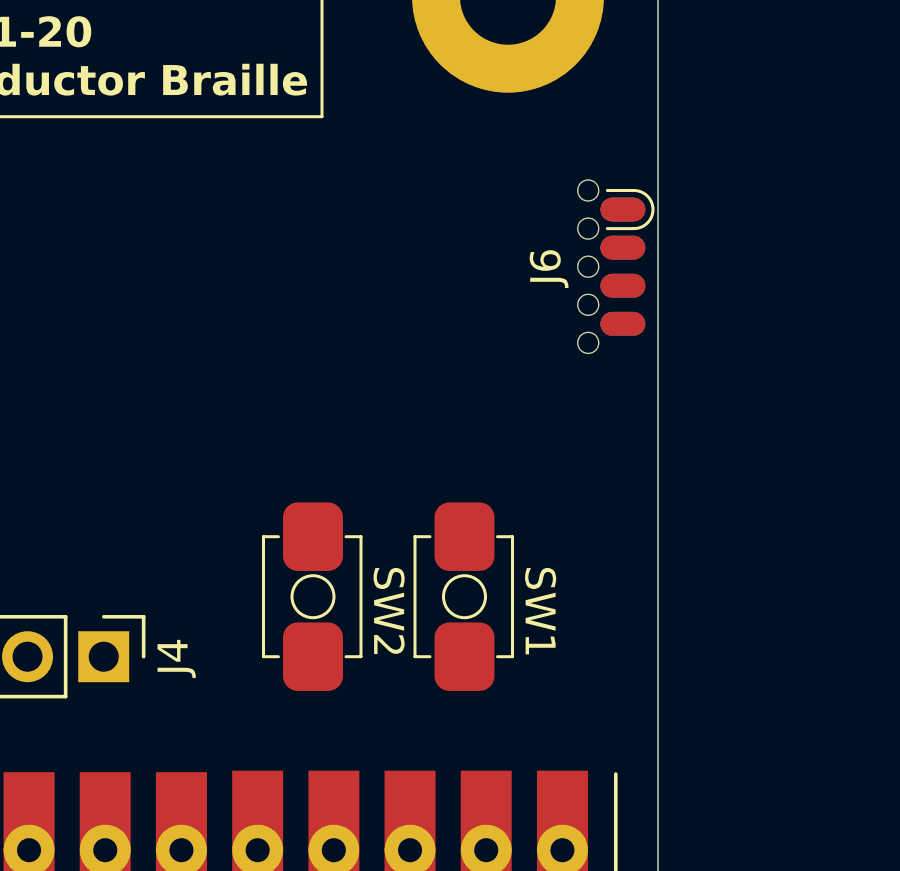
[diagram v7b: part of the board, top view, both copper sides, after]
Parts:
- added J6: Conn_01x08, 00-project-footprints:SOICbite_clipProgSmall, F.Cu at (119.6, 44.0)
- moved SW1 3.05 mm to (113.5, 55.0)
- moved SW2 3.05 mm to (108.5, 55.0)
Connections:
- net Net-(J5-Pin_1) renamed /UART0_TX
- net Net-(J5-Pin_2) renamed /UART0_RX
